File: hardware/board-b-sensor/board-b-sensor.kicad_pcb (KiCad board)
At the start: 2 copper layers, 18 x 14 mm, 7 parts, among them J1 Conn_01x08, U1 ICM-42688-P

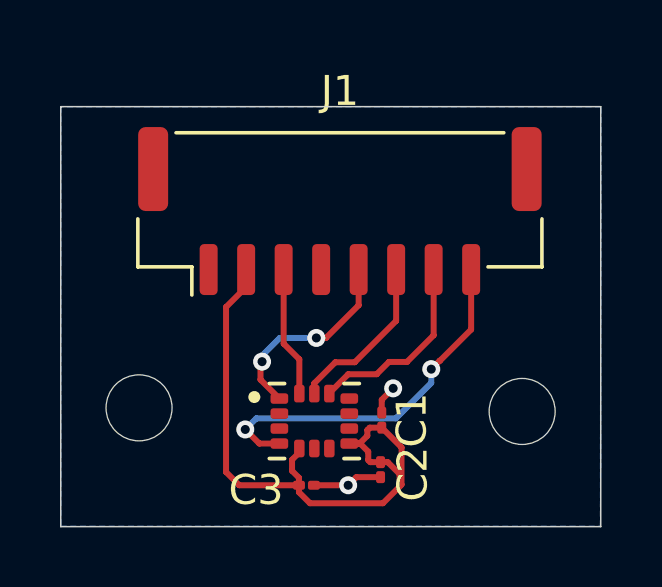
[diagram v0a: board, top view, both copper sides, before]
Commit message: Add exported schematics, PCB layouts, and BOM
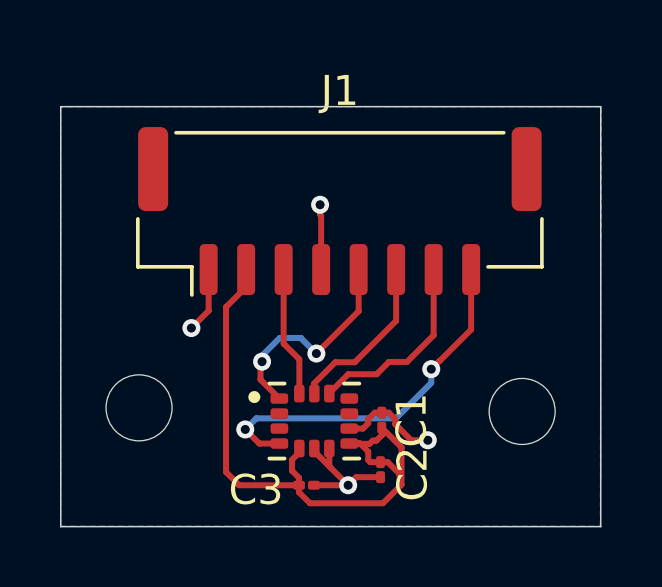
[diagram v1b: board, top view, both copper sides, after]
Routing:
- net GND: track 3.30 -> 12.4 mm, vias 2 -> 4
- net /IMU_SPI_MISO: track 6.82 -> 7.37 mm
- added copper zone on B.Cu, net GND
- removed copper zone on B.Cu, net (none)
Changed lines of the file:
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@@
 	)
 	(segment
-		(start 153.335 108.58)
-		(end 153.335 108.15)
+		(start 151.5875 110.3725)
+		(end 151.5875 109.775)
+		(width 0.2)
+		(layer "F.Cu")
+		(net "GND")
+	)
+	(segment
+		(start 147.565 103.81)
+		(end 147.565 105.185)
+		(width 0.2)
+		(layer "F.Cu")
+		(net "GND")
+	)
+	(segment
+		(start 152.71 109.11)
+		(end 152.885 108.935)
+		(width 0.2)
+		(layer "F.Cu")
+		(net "GND")
+	)
+	(segment
+		(start 151.0875 109.775)
+		(end 151.0625 109.8)
+		(width 0.2)
+		(layer "F.Cu")
+		(net "GND")
+	)
+	(segment
+		(start 153.785 108.79759)
+		(end 153.56741 108.58)
+		(width 0.2)
+		(layer "F.Cu")
+		(net "GND")
+	)
+	(segment
+		(start 152.215 111)
+		(end 151.5875 110.3725)
+		(width 0.2)
+		(layer "F.Cu")
+		(net "GND")
+	)
+	(segment
+		(start 152.885 108.935)
+		(end 152.885 108.79759)
+		(width 0.2)
+		(layer "F.Cu")
+		(net "GND")
+	)
+	(segment
+		(start 154.320686 109.5)
+		(end 153.785 108.964314)
 		(width 0.2)
 		(layer "F.Cu")
@@
 	)
 	(segment
+		(start 151.28 101.98)
+		(end 151.315 102.015)
+		(width 0.2)
+		(layer "F.Cu")
+		(net "GND")
+	)
+	(segment
+		(start 153.10259 108.58)
+		(end 153.335 108.58)
+		(width 0.2)
+		(layer "F.Cu")
+		(net "GND")
+	)
+	(segment
+		(start 152.885 108.79759)
+		(end 153.10259 108.58)
+		(width 0.2)
+		(layer "F.Cu")
+		(net "GND")
+	)
+	(segment
+		(start 152.2525 109.11)
+		(end 152.71 109.11)
+		(width 0.2)
+		(layer "F.Cu")
+		(net "GND")
+	)
+	(segment
+		(start 147.565 105.185)
+		(end 146.99 105.76)
+		(width 0.2)
+		(layer "F.Cu")
+		(net "GND")
+	)
+	(segment
+		(start 151.0625 109.8475)
+		(end 151.5875 110.3725)
+		(width 0.2)
+		(layer "F.Cu")
+		(net "GND")
+	)
+	(segment
 		(start 152.485 110.73)
 		(end 152.215 111)
@@
 	)
 	(segment
-		(start 153.335 108.15)
-		(end 153.715 107.77)
+		(start 151.0625 109.8)
+		(end 151.0625 109.8475)
 		(width 0.2)
 		(layer "F.Cu")
@@
 		(net "GND")
 	)
-	(via
-		(at 153.715 107.77)
+	(segment
+		(start 151.28 101.65)
+		(end 151.28 101.98)
+		(width 0.2)
+		(layer "F.Cu")
+		(net "GND")
+	)
+	(segment
+		(start 153.785 108.964314)
+		(end 153.785 108.79759)
+		(width 0.2)
+		(layer "F.Cu")
+		(net "GND")
+	)
+	(segment
+		(start 153.56741 108.58)
+		(end 153.335 108.58)
+		(width 0.2)
+		(layer "F.Cu")
+		(net "GND")
+	)
+	(segment
+		(start 154.87 109.5)
+		(end 154.320686 109.5)
+		(width 0.2)
+		(layer "F.Cu")
+		(net "GND")
+	)
+	(segment
+		(start 151.315 102.015)
+		(end 151.315 103.81)
+		(width 0.2)
+		(layer "F.Cu")
+		(net "GND")
+	)
+	(via
+		(at 154.87 109.5)
 		(size 0.6)
 		(drill 0.3)
@@
 	(via
 		(at 152.215 111)
+		(size 0.6)
+		(drill 0.3)
+		(layers "F.Cu" "B.Cu")
+		(net "GND")
+	)
+	(via
+		(at 151.28 101.65)
+		(size 0.6)
+		(drill 0.3)
+		(layers "F.Cu" "B.Cu")
+		(net "GND")
+	)
+	(via
+		(at 146.99 105.76)
 		(size 0.6)
 		(drill 0.3)
@@
 	)
 	(segment
+		(start 153.157068 109.512932)
+		(end 153.36 109.31)
+		(width 0.2)
+		(layer "F.Cu")
+		(net "/3.3V")
+	)
+	(segment
 		(start 152.615 109.61)
 		(end 152.885 109.88)
@@
 	)
 	(segment
+		(start 152.93 109.62)
+		(end 153.037068 109.512932)
+		(width 0.2)
+		(layer "F.Cu")
+		(net "/3.3V")
+	)
+	(segment
 		(start 153.995 109.74)
 		(end 153.335 109.08)
@@
 	)
 	(segment
+		(start 152.2525 109.61)
+		(end 152.597932 109.61)
+		(width 0.2)
+		(layer "F.Cu")
+		(net "/3.3V")
+	)
+	(segment
 		(start 153.535 110.23)
 		(end 153.93 110.625)
@@
 	)
 	(segment
+		(start 153.36 109.105)
+		(end 153.335 109.08)
+		(width 0.2)
+		(layer "F.Cu")
+		(net "/3.3V")
+	)
+	(segment
 		(start 148.815 104.39)
 		(end 148.815 103.81)
@@
 	)
 	(segment
-		(start 152.855 109.352932)
-		(end 152.855 109.16)
-		(width 0.2)
-		(layer "F.Cu")
-		(net "/3.3V")
-	)
-	(segment
-		(start 152.2525 109.61)
-		(end 152.597932 109.61)
-		(width 0.2)
-		(layer "F.Cu")
-		(net "/3.3V")
-	)
-	(segment
 		(start 150.575 111)
 		(end 150.575 111.23241)
@@
 	)
 	(segment
-		(start 152.935 109.08)
-		(end 153.335 109.08)
-		(width 0.2)
-		(layer "F.Cu")
-		(net "/3.3V")
-	)
-	(segment
 		(start 153.375 111.6)
 		(end 153.93 111.045)
@@
 	)
 	(segment
-		(start 152.855 109.16)
-		(end 152.935 109.08)
+		(start 153.36 109.31)
+		(end 153.36 109.105)
+		(width 0.2)
+		(layer "F.Cu")
+		(net "/3.3V")
+	)
+	(segment
+		(start 152.597932 109.61)
+		(end 152.607932 109.62)
 		(width 0.2)
 		(layer "F.Cu")
@@
 	)
 	(segment
+		(start 152.607932 109.62)
+		(end 152.93 109.62)
+		(width 0.2)
+		(layer "F.Cu")
+		(net "/3.3V")
+	)
+	(segment
 		(start 152.885 109.88)
 		(end 152.885 110.16)
@@
 	)
 	(segment
-		(start 152.597932 109.61)
-		(end 152.855 109.352932)
+		(start 153.037068 109.512932)
+		(end 153.157068 109.512932)
 		(width 0.2)
 		(layer "F.Cu")
@@
 	)
 	(segment
-		(start 151.475 106.09)
-		(end 152.565 105)
-		(width 0.2)
-		(layer "F.Cu")
-		(net "/IMU_SPI_MISO")
-	)
-	(segment
 		(start 149.2925 106.9325)
 		(end 149.2925 107.48)
@@
 	)
 	(segment
-		(start 152.565 105)
+		(start 152.565 105.200463)
 		(end 152.565 103.81)
 		(width 0.2)
@@
 	)
 	(segment
-		(start 151.155 106.09)
-		(end 151.475 106.09)
+		(start 151.155701 106.609762)
+		(end 152.565 105.200463)
 		(width 0.2)
 		(layer "F.Cu")
@@
 	)
 	(via
-		(at 151.155 106.09)
-		(size 0.6)
-		(drill 0.3)
-		(layers "F.Cu" "B.Cu")
-		(net "/IMU_SPI_MISO")
-	)
-	(segment
-		(start 151.155 106.09)
+		(at 151.155701 106.609762)
+		(size 0.6)
+		(drill 0.3)
+		(layers "F.Cu" "B.Cu")
+		(net "/IMU_SPI_MISO")
+	)
+	(segment
+		(start 150.635939 106.09)
 		(end 149.935 106.09)
+		(width 0.2)
+		(layer "B.Cu")
+		(net "/IMU_SPI_MISO")
+	)
+	(segment
+		(start 151.155701 106.609762)
+		(end 150.635939 106.09)
+		(width 0.2)
+		(layer "B.Cu")
+		(net "/IMU_SPI_MISO")
+	)
+	(segment
+		(start 149.935 106.09)
+		(end 149.345 106.68)
 		(width 0.2)
 		(layer "B.Cu")
@@
 	)
 	(segment
-		(start 149.935 106.09)
-		(end 149.345 106.68)
-		(width 0.2)
-		(layer "B.Cu")
-		(net "/IMU_SPI_MISO")
-	)
-	(segment
 		(start 155.265 106.85)
 		(end 155.275 106.85)
@@
 	)
 	(zone
+		(net "GND")
 		(layer "B.Cu")
 		(hatch edge 0.5)
